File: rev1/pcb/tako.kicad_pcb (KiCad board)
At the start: 2 copper layers, 230.7 x 97.8 mm, 120 parts, among them J1 MJ-4PP-9, J101 MJ-4PP-9, SW1 EC_SW, SW10 EC_SW, SW101 EC_SW, SW102 EC_SW, SW103 EC_SW, SW104 EC_SW, SW105 EC_SW, SW106 EC_SW, SW107 EC_SW, SW108 EC_SW, SW109 EC_SW, SW11 EC_SW, SW110 EC_SW, SW111 EC_SW, SW112 EC_SW, SW113 EC_SW, SW114 EC_SW, SW115 EC_SW, SW116 EC_SW, SW117 EC_SW, SW12 EC_SW, SW13 EC_SW, SW14 EC_SW, SW15 EC_SW, SW16 EC_SW, SW17 EC_SW, SW2 EC_SW, SW3 EC_SW, SW4 EC_SW, SW5 EC_SW, SW6 EC_SW, SW7 EC_SW, SW8 EC_SW, SW9 EC_SW, U1 STeMCell, U101 STeMCell, U102 74HC4051, U103 OPA350, U2 74HC4051, U3 OPA350

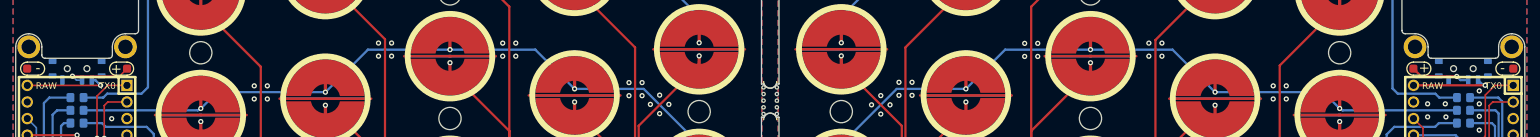
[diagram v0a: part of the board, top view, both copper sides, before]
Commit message: Expose bat pads on both front and back sides
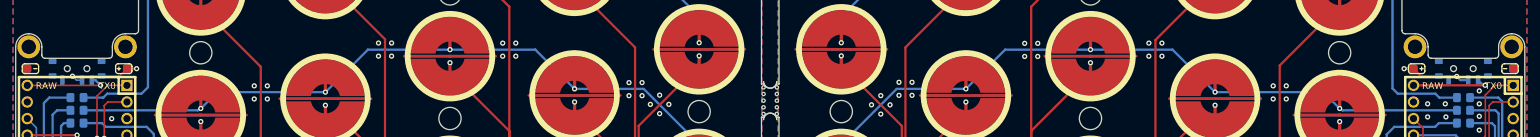
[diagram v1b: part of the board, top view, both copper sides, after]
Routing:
- net BAT+_R: track 10.5 -> 13.5 mm, vias 1 -> 2
- net BAT+: track 9.11 -> 12.0 mm, vias 1 -> 2

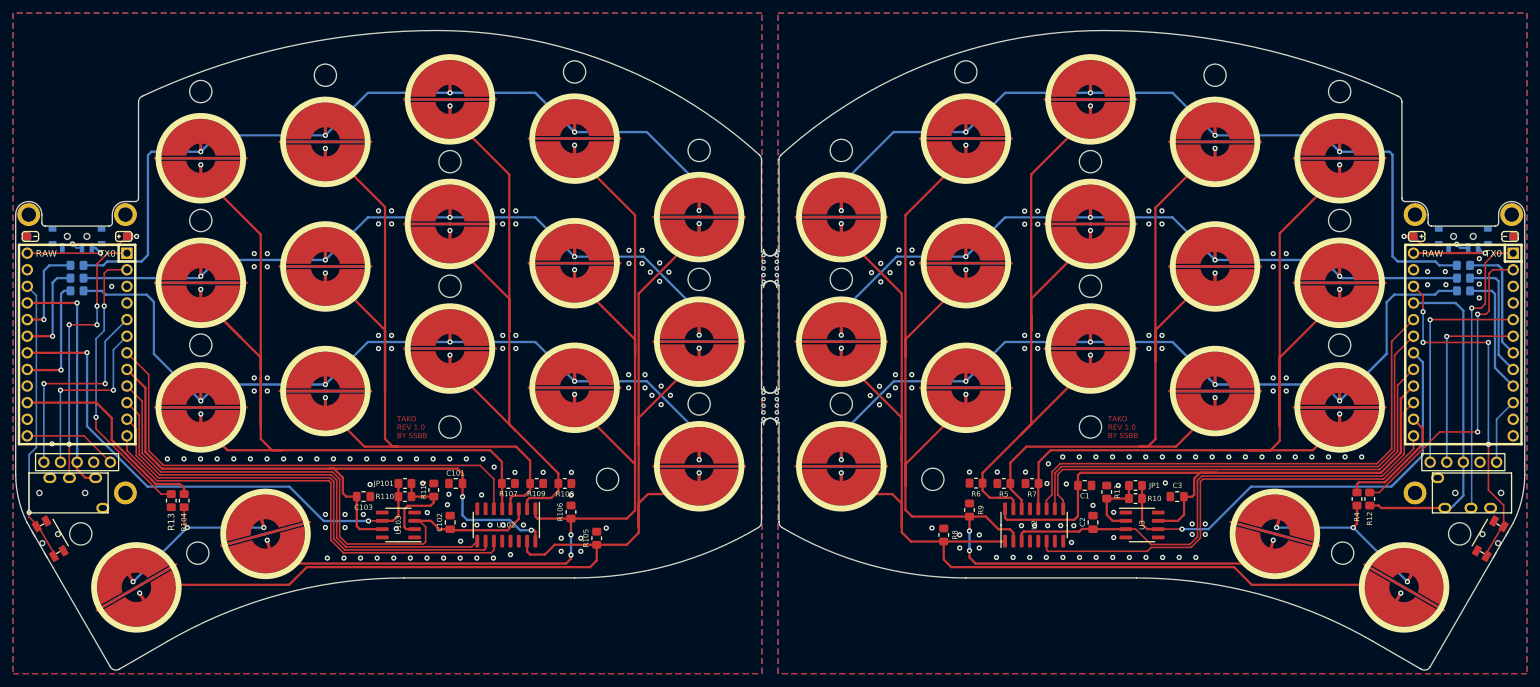
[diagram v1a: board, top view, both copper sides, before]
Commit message: Add build guide components section
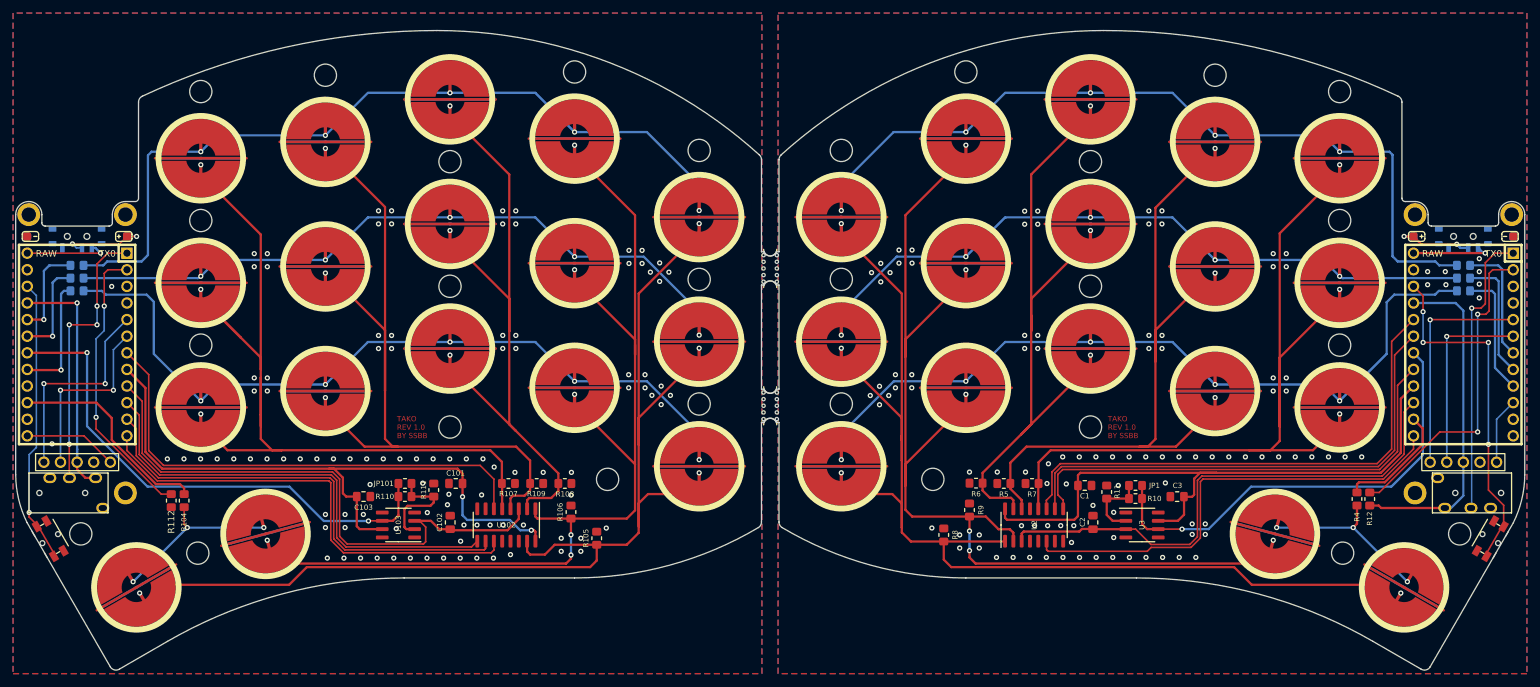
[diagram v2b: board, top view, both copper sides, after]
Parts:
- R112: renamed from R13; value 10k -> 5.1k
- R12: value 10k -> 5.1k
